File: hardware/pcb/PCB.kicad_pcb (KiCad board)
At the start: 2 copper layers, 53 x 93 mm, 44 parts, among them J1 USB_A, J2 AudioJack3, J3 USB_B_Micro, Q1 BSS138, Q2 S8050, Q3 S8050, SW1 SW_RESET, SW2 S4_SW, U1 ESP32-S3-WROOM-1, U2 LM3525M-H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

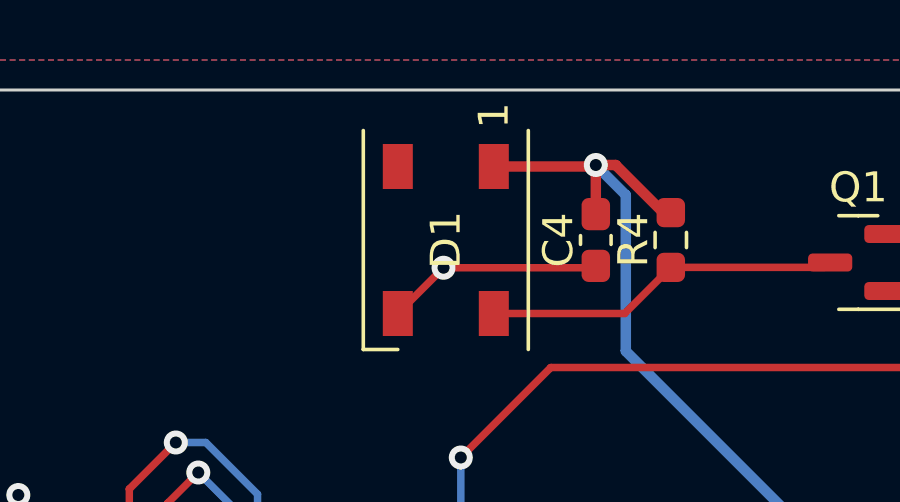
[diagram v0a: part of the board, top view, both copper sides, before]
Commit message: swap led part#
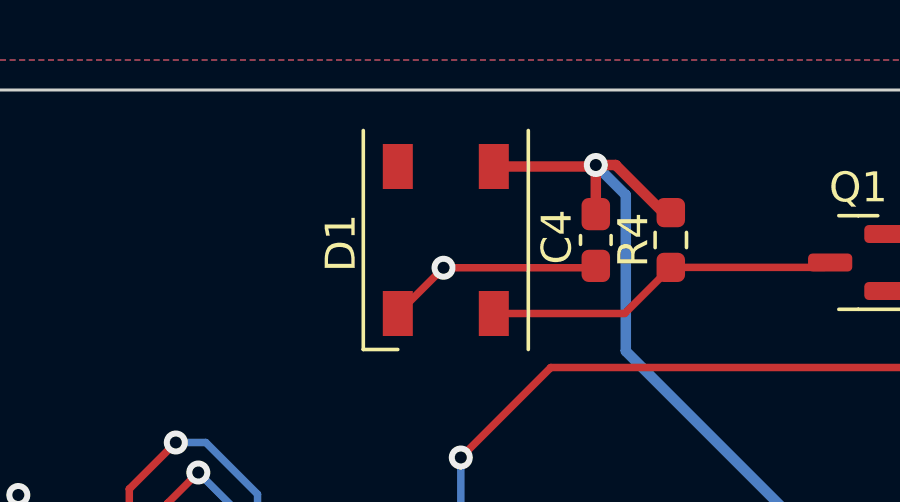
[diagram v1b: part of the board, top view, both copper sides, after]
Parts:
- D1: value WS2812B -> SK6812; footprint LED_SMD:LED_WS2812B_PLCC4_5.0x5.0mm_P3.2mm -> LED_SMD:LED_SK6812_PLCC4_5.0x5.0mm_P3.2mm
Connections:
- D1 pad 1: VBUS -> Earth
- D1 pad 2: unconnected-(D1-Pad2) -> Net-(Q1-Pad3)
- D1 pad 3: Earth -> VBUS
- D1 pad 4: Net-(D1-Pad4) -> unconnected-(D1-Pad4)
- Q1 pad 3: Net-(D1-Pad4) -> Net-(Q1-Pad3)
- R4 pad 1: Net-(D1-Pad4) -> Net-(Q1-Pad3)
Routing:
- net Net-(Q1-Pad3): track 0.00 -> 11.7 mm
- net Net-(D1-Pad4): track 11.7 -> 0.00 mm

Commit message: board updates
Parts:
- Q2, Q3: value S8050 -> MMBT3904
- R3, R6: value 10k -> 10K
- turned D2 to -90 degrees
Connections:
- D2 pad 1: ESD_VBUS -> VBUS
- D2 pad 2: VBUS -> ESD_VBUS
- R11 pad 1: Net-(Q2-Pad1) -> Net-(Q2-Pad2)
- R11 pad 2: Net-(Q3-Pad2) -> Net-(Q3-Pad1)
- R8 pad 1: Net-(Q3-Pad1) -> Net-(Q3-Pad2)
- R8 pad 2: Net-(Q2-Pad2) -> Net-(Q2-Pad1)
- U4 pad 19: Net-(Q3-Pad1) -> Net-(Q3-Pad2)
- U4 pad 20: U0_RXD -> U0_TXD
- U4 pad 21: U0_TXD -> U0_RXD
- U4 pad 23: Net-(Q2-Pad1) -> Net-(Q2-Pad2)
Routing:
- net Net-(Q2-Pad2): track 9.98 -> 28.8 mm, vias 0 -> 2
- net Net-(Q2-Pad1): track 25.6 -> 9.10 mm, vias 2 -> 0
- net Net-(Q3-Pad1): track 13.2 -> 5.16 mm
- net Net-(Q3-Pad2): track 4.18 -> 12.2 mm
- net U0_RXD: track 48.1 -> 52.8 mm
- net U0_TXD: track 53.2 -> 50.2 mm
- net CHIP_PU: track 91.2 -> 91.8 mm
- net Earth: vias 25 -> 29
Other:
- board size 53 x 93 mm -> 55 x 95 mm
- board text added: "RESET"

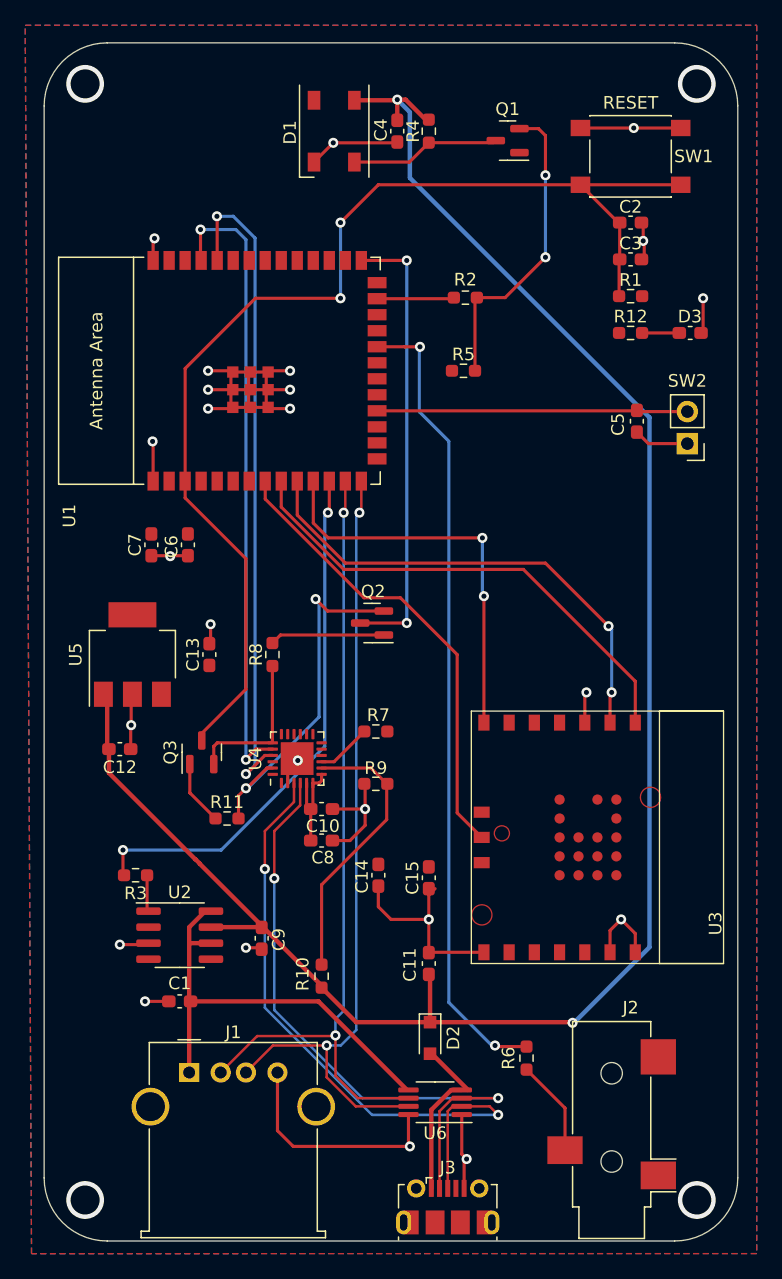
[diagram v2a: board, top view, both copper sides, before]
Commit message: Revision 2: Fixed auto program transistor pins Fixed TX/RX to U0 Increased board size Added screw holes Added BOOT switch Added RESET jumper
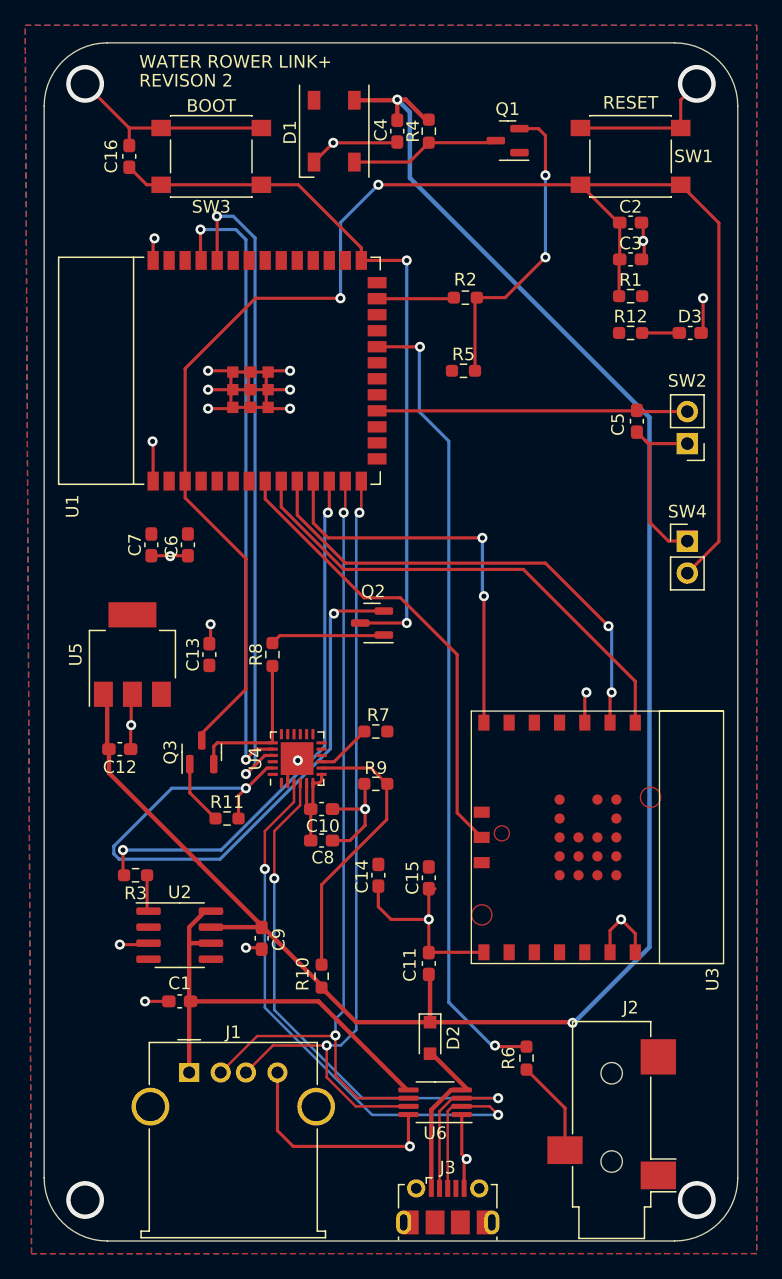
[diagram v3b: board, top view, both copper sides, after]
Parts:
- added C16: 0.1uF, Capacitor_SMD:C_0603_1608Metric_Pad1.08x0.95mm_HandSolder, F.Cu at (105.8, 94.0)
- added SW3: BOOT, Button_Switch_SMD:SW_Push_1P1T_NO_6x6mm_H9.5mm, F.Cu at (112.2, 94.0)
- added SW4: RESET, Connector_PinHeader_2.54mm:PinHeader_1x02_P2.54mm_Vertical, F.Cu at (150.0, 124.5)
- SW1: value SW_RESET -> RESET
- SW2: value S4_SW -> S4
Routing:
- net CHIP_PU: track 91.8 -> 124.3 mm
- net Earth: track 129.6 -> 160.5 mm, vias 29 -> 28
- net Net-(Q2-Pad2): track 28.8 -> 54.3 mm
- net BOOT: track 36.0 -> 58.1 mm
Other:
- board text added: "BOOT"
- board text added: "REVISON 2"
- board text added: "WATER ROWER LINK+"

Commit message: moved CP210N via
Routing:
- net Earth: track 160.5 -> 163.6 mm
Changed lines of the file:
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@@
   (segment (start 127.8875 169.975) (end 127.8875 172.3875) (width 0.25) (layer "F.Cu") (net 6))
   (segment (start 132.5 173.5) (end 132.3 173.7) (width 0.25) (layer "F.Cu") (net 6))
+  (segment (start 118.3125 144.27548) (end 118.3125 143.6875) (width 0.25) (layer "F.Cu") (net 6))
   (segment (start 129.5 154.5) (end 129.5 152.5625) (width 0.25) (layer "F.Cu") (net 6))
   (segment (start 121.925 92.925) (end 126.5625 92.925) (width 0.25) (layer "F.Cu") (net 6))
@@
   (segment (start 129.5 152.5625) (end 130 152.0625) (width 0.25) (layer "F.Cu") (net 6))
   (segment (start 112.2 131.1) (end 112.2 132.7375) (width 0.25) (layer "F.Cu") (net 6))
+  (segment (start 117.83798 144.75) (end 118.3125 144.27548) (width 0.25) (layer "F.Cu") (net 6))
   (segment (start 107.64 100.61) (end 107.64 102.25) (width 0.25) (layer "F.Cu") (net 6))
   (segment (start 143.8715 155.3785) (end 144.75 154.5) (width 0.25) (layer "F.Cu") (net 6))
   (segment (start 109.0375 125.6625) (end 109 125.7) (width 0.25) (layer "F.Cu") (net 6))
   (segment (start 105 156.5) (end 107.16 156.5) (width 0.25) (layer "F.Cu") (net 6))
+  (segment (start 116 144.75) (end 117.83798 144.75) (width 0.25) (layer "F.Cu") (net 6))
   (segment (start 124.4495 145.75) (end 124.4495 147.0505) (width 0.25) (layer "F.Cu") (net 6))
   (segment (start 117.5 166.64) (end 117.5 171.25) (width 0.25) (layer "F.Cu") (net 6))
@@
   (via (at 132.5 173.5) (size 0.8) (drill 0.4) (layers "F.Cu" "B.Cu") (free) (net 6))
   (via (at 128 172.5) (size 0.8) (drill 0.4) (layers "F.Cu" "B.Cu") (free) (net 6))
-  (via (at 119.1125 141.9) (size 0.8) (drill 0.4) (layers "F.Cu" "B.Cu") (net 6))
   (via (at 107.6 116.6) (size 0.8) (drill 0.4) (layers "F.Cu" "B.Cu") (free) (net 6))
   (via (at 118.5 111) (size 0.8) (drill 0.4) (layers "F.Cu" "B.Cu") (free) (net 6))
   (via (at 146.5 100.7) (size 0.8) (drill 0.4) (layers "F.Cu" "B.Cu") (free) (net 6))
+  (via (at 116 144.75) (size 0.8) (drill 0.4) (layers "F.Cu" "B.Cu") (free) (net 6))
   (via (at 105 156.5) (size 0.8) (drill 0.4) (layers "F.Cu" "B.Cu") (free) (net 6))
   (via (at 112 111) (size 0.8) (drill 0.4) (layers "F.Cu" "B.Cu") (free) (net 6))

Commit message: R3 PCB
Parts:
- moved D3 63.6 mm to (151.6, 171.6), turned to 90 degrees
- moved R12 59.7 mm to (151.6, 167.4), turned to 90 degrees
- moved SW3 39.7 mm to (149.6, 107.5), turned to -90 degrees
- moved C16 38.6 mm to (141.2, 109.2), turned to 180 degrees
- moved C2 15.4 mm to (141.2, 114.0), turned to 0 degrees
- moved C5 13.6 mm to (132.4, 114.0), turned to 0 degrees
- moved R1 12.5 mm to (136.8, 114.0)
- moved C3 11.2 mm to (136.8, 109.2)
- moved SW2 9.80 mm to (152.2, 126.3), turned to 0 degrees
- moved SW4 5.49 mm to (152.2, 119.5), turned to 180 degrees
- moved SW1 4.48 mm to (149.6, 95.8), turned to -90 degrees
- moved R5 1.81 mm to (132.4, 109.2)
- moved C7 0.10 mm to (107.6, 124.8), turned to 90 degrees
- turned C6 to 90 degrees
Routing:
- net Net-(Q2-Pad2): track 54.3 -> 26.9 mm
- net VBUS: track 150.7 -> 126.8 mm
- net Earth: track 163.6 -> 179.6 mm, vias 28 -> 21
- net BOOT: track 58.1 -> 70.3 mm
- net Net-(C5-Pad1): track 24.5 -> 34.0 mm, vias 0 -> 2
- net CHIP_PU: track 124.3 -> 126.3 mm, vias 2 -> 4
- net Net-(Q1-Pad2): track 24.4 -> 23.1 mm
- net Net-(R3-Pad2): track 42.6 -> 41.7 mm
- net Net-(D3-Pad2): track 2.95 -> 2.43 mm
- net Net-(R10-Pad2): vias 0 -> 2
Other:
- board text added: "REVISON 3"
- board text added: "S4_PWR"
- board text removed: "BOOT"
- board text removed: "REVISON 2"
